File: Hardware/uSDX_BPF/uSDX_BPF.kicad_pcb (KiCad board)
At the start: 2 copper layers, 44.5 x 14 mm, 18 parts

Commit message: updated the 3D models
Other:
- net class Default removed

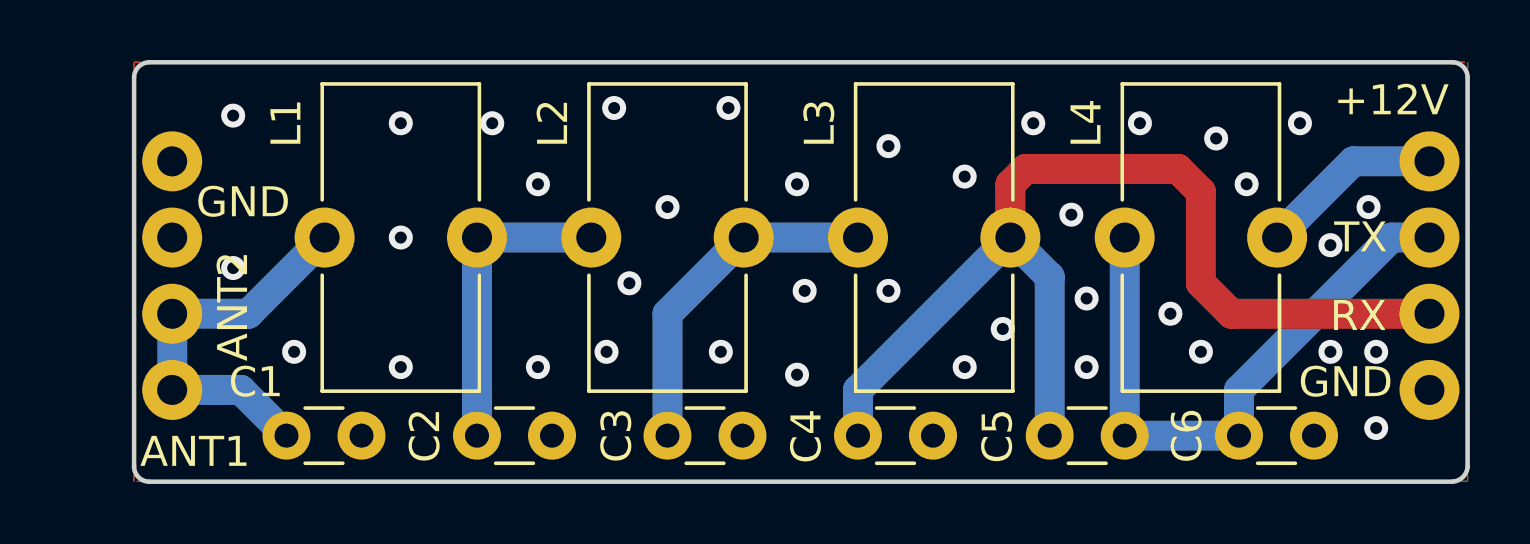
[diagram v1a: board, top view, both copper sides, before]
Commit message: updated the project with transferrable libraries
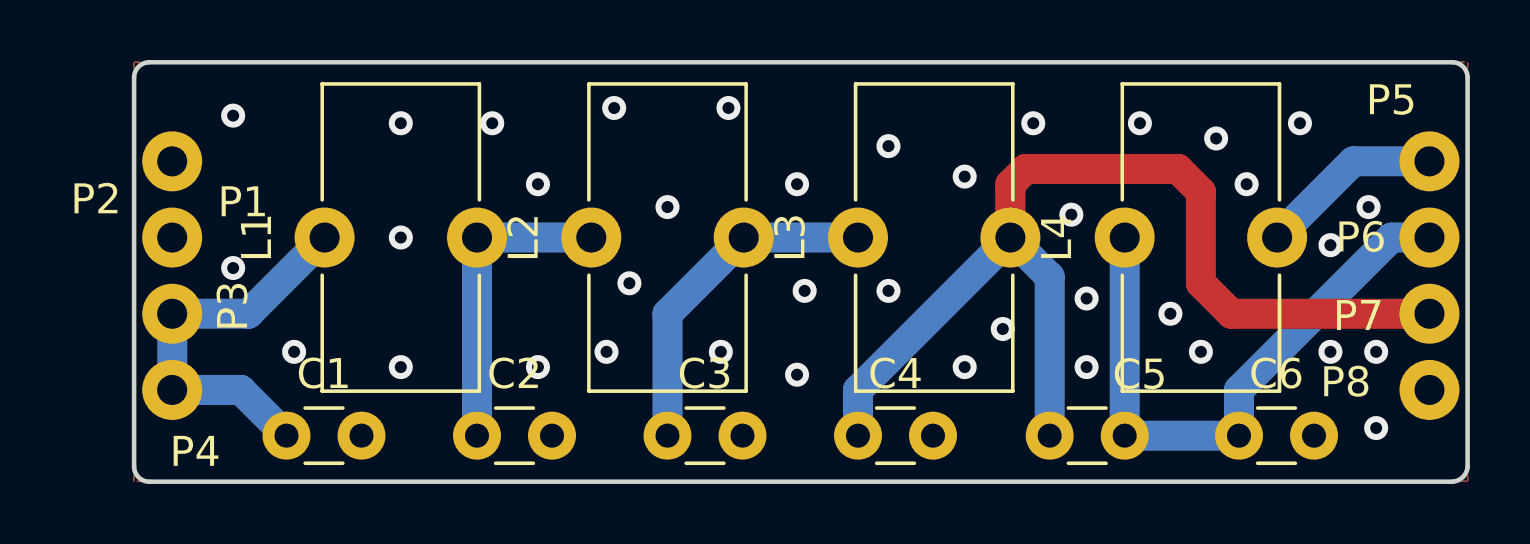
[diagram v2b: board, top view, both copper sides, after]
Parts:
- C1, C2: footprint Capacitor_THT:C_Disc_D3.0mm_W1.6mm_P2.50mm -> user_footprints:C_Disc_D3.0mm_W1.6mm_P2.50mm
- C3: value (none) -> 390pF; footprint Capacitor_THT:C_Disc_D3.0mm_W1.6mm_P2.50mm -> user_footprints:C_Disc_D3.0mm_W1.6mm_P2.50mm
- C4: value (none) -> 180pF; footprint Capacitor_THT:C_Disc_D3.0mm_W1.6mm_P2.50mm -> user_footprints:C_Disc_D3.0mm_W1.6mm_P2.50mm
- C5: value (none) -> 100nF; footprint Capacitor_THT:C_Disc_D3.0mm_W1.6mm_P2.50mm -> user_footprints:C_Disc_D3.0mm_W1.6mm_P2.50mm
- C6: value (none) -> 30pF; footprint Capacitor_THT:C_Disc_D3.0mm_W1.6mm_P2.50mm -> user_footprints:C_Disc_D3.0mm_W1.6mm_P2.50mm
- L1, L2, L3: footprint Inductor_THT:L_Toroid_Vertical_L10.0mm_W5.0mm_P5.08mm -> user_footprints:L_Toroid_Vertical_L10.0mm_W5.0mm_P5.08mm
- L4: value (none) -> T50-2 (9T); footprint Inductor_THT:L_Toroid_Vertical_L10.0mm_W5.0mm_P5.08mm -> user_footprints:L_Toroid_Vertical_L10.0mm_W5.0mm_P5.08mm
- P1, P8: renamed from GND; value (none) -> GND
- P2: renamed from  ; value (none) -> GND
- P3: renamed from ANT2; value (none) -> ANT2
- P4: renamed from ANT1; value (none) -> ANT1
- P5: renamed from +12V; value (none) -> +12V
- P7: renamed from RX; value (none) -> RX
- renumbered TX to P6

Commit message: update library locations
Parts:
- moved P5 2.70 mm to (97.8, 36.5)
- moved P6 1.10 mm to (97.8, 39.1)
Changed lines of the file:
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@@
   )
   (footprint "user_footprints:pin" (layer "F.Cu")
-    (at 95.09 36.5252)
-    (property "Sheetfile" "uSDX_BPF.kicad_sch")
-    (property "Sheetname" "")
-    (attr through_hole)
-    (fp_text reference "P5" (at 1.43 -2.2352) (layer "F.SilkS")
-      (effects (font (size 1 1) (thickness 0.15)))
-    )
-    (fp_text value "+12V" (at -4.91 -1.3932) (layer "F.Fab")
-      (effects (font (size 1 1) (thickness 0.15)))
-    )
-    (pad "1" thru_hole circle locked (at 2.7 -0.2032) (size 2 2) (drill 1) (layers *.Cu *.Mask)
+    (at 97.79 36.5252)
+    (property "Sheetfile" "uSDX_BPF.kicad_sch")
+    (property "Sheetname" "")
+    (attr through_hole)
+    (fp_text reference "P5" (at 0 -2.54) (layer "F.SilkS")
+      (effects (font (size 0.8 0.8) (thickness 0.1)))
+    )
+    (fp_text value "+12V" (at 0 -5.08) (layer "F.Fab")
+      (effects (font (size 0.8 0.8) (thickness 0.1)))
+    )
+    (pad "1" thru_hole circle (at 0 -0.2032) (size 2 2) (drill 1) (layers *.Cu *.Mask)
       (net 7 "Net-(L4-Pad2)") (pintype "unspecified"))
-    (model "C:/Users/Liviu/Documents/Projects/uSDX_variant/Hardware/3D_models/filterStandoff.step"
-      (offset (xyz 2.7 0 0))
+    (model "${KICAD6_3DMODEL_DIR}/filterStandoff.step"
+      (offset (xyz 0 0 0))
       (scale (xyz 1 1 1))
       (rotate (xyz 0 0 0))
@@
     (property "Sheetname" "")
     (attr through_hole)
-    (fp_text reference "P7" (at -2.37 -0.1232) (layer "F.SilkS")
-      (effects (font (size 1 1) (thickness 0.15)))
-    )
-    (fp_text value "RX" (at -3.64 -0.1232) (layer "F.Fab")
-      (effects (font (size 1 1) (thickness 0.15)))
-    )
-    (pad "1" thru_hole circle locked (at 0 -0.2032) (size 2 2) (drill 1) (layers *.Cu *.Mask)
+    (fp_text reference "P7" (at 0 -2.54) (layer "F.SilkS")
+      (effects (font (size 0.8 0.8) (thickness 0.1)))
+    )
+    (fp_text value "RX" (at 0 -5.08) (layer "F.Fab")
+      (effects (font (size 0.8 0.8) (thickness 0.1)))
+    )
+    (pad "1" thru_hole circle (at 0 -0.2032) (size 2 2) (drill 1) (layers *.Cu *.Mask)
       (net 5 "Net-(C4-Pad1)") (pintype "unspecified"))
-    (model "C:/Users/Liviu/Documents/Projects/uSDX_variant/Hardware/3D_models/filterStandoff.step"
+    (model "${KICAD6_3DMODEL_DIR}/filterStandoff.step"
       (offset (xyz 0 0 0))
       (scale (xyz 1 1 1))
@@
     (property "Sheetname" "")
     (attr through_hole)
-    (fp_text reference "P8" (at -2.794 -0.4572) (layer "F.SilkS")
-      (effects (font (size 1 1) (thickness 0.15)))
-    )
-    (fp_text value "GND" (at -2.37 -0.1232) (layer "F.Fab")
-      (effects (font (size 1 1) (thickness 0.15)))
-    )
-    (pad "1" thru_hole circle locked (at 0 -0.2032) (size 2 2) (drill 1) (layers *.Cu *.Mask)
+    (fp_text reference "P8" (at 0 -2.54) (layer "F.SilkS")
+      (effects (font (size 0.8 0.8) (thickness 0.1)))
+    )
+    (fp_text value "GND" (at 0 -5.08) (layer "F.Fab")
+      (effects (font (size 0.8 0.8) (thickness 0.1)))
+    )
+    (pad "1" thru_hole circle (at 0 -0.2032) (size 2 2) (drill 1) (layers *.Cu *.Mask)
       (net 1 "GND") (pintype "unspecified"))
     (model "${KICAD6_3DMODEL_DIR}/filterStandoff.step"
@@
     (property "Sheetname" "")
     (attr through_hole)
-    (fp_text reference "P4" (at 0.765353 1.864672) (layer "F.SilkS")
-      (effects (font (size 1 1) (thickness 0.15)))
-    )
-    (fp_text value "ANT1" (at -3.81 -0.2032) (layer "F.Fab")
-      (effects (font (size 1 1) (thickness 0.15)))
-    )
-    (pad "1" thru_hole circle locked (at 0 -0.2032) (size 2 2) (drill 1) (layers *.Cu *.Mask)
+    (fp_text reference "P4" (at 0 -2.54) (layer "F.SilkS")
+      (effects (font (size 0.8 0.8) (thickness 0.1)))
+    )
+    (fp_text value "ANT1" (at 0 -5.08) (layer "F.Fab")
+      (effects (font (size 0.8 0.8) (thickness 0.1)))
+    )
+    (pad "1" thru_hole circle (at 0 -0.2032) (size 2 2) (drill 1) (layers *.Cu *.Mask)
       (net 2 "Net-(C1-Pad1)") (pintype "unspecified"))
-    (model "C:/Users/Liviu/Documents/Projects/uSDX_variant/Hardware/3D_models/filterStandoff.step"
+    (model "${KICAD6_3DMODEL_DIR}/filterStandoff.step"
       (offset (xyz 0 0 0))
       (scale (xyz 1 1 1))
@@
     (property "Sheetname" "")
     (attr through_hole)
-    (fp_text reference "P2" (at -2.54 -1.4732) (layer "F.SilkS")
-      (effects (font (size 1 1) (thickness 0.15)))
-    )
-    (fp_text value "GND" (at -2.54 -0.2032) (layer "F.Fab")
-      (effects (font (size 1 1) (thickness 0.15)))
-    )
-    (pad "1" thru_hole circle locked (at 0 -0.2032) (size 2 2) (drill 1) (layers *.Cu *.Mask)
+    (fp_text reference "P2" (at 0 -2.54) (layer "F.SilkS")
+      (effects (font (size 0.8 0.8) (thickness 0.1)))
+    )
+    (fp_text value "GND" (at 0 -5.08) (layer "F.Fab")
+      (effects (font (size 0.8 0.8) (thickness 0.1)))
+    )
+    (pad "1" thru_hole circle (at 0 -0.2032) (size 2 2) (drill 1) (layers *.Cu *.Mask)
       (net 1 "GND") (pintype "unspecified"))
-    (model "C:/Users/Liviu/Documents/Projects/uSDX_variant/Hardware/3D_models/filterStandoff.step"
-      (offset (xyz 0 0 0))
-      (scale (xyz 1 1 1))
-      (rotate (xyz 0 0 0))
-    )
-  )
-  (footprint "user_footprints:pin" (layer "F.Cu")
-    (at 96.69 39.0652)
-    (property "Sheetfile" "uSDX_BPF.kicad_sch")
-    (property "Sheetname" "")
-    (attr through_hole)
-    (fp_text reference "P6" (at -1.186 -0.2032) (layer "F.SilkS")
-      (effects (font (size 1 1) (thickness 0.15)))
-    )
-    (fp_text value "TX" (at -3.64 -0.1232) (layer "F.Fab")
-      (effects (font (size 1 1) (thickness 0.15)))
-    )
-    (pad "1" thru_hole circle locked (at 1.1 -0.2032) (size 2 2) (drill 1) (layers *.Cu *.Mask)
+    (model "${KICAD6_3DMODEL_DIR}/filterStandoff.step"
+      (offset (xyz 0 0 0))
+      (scale (xyz 1 1 1))
+      (rotate (xyz 0 0 0))
+    )
+  )
+  (footprint "user_footprints:pin" (layer "F.Cu")
+    (at 97.79 39.0652)
+    (property "Sheetfile" "uSDX_BPF.kicad_sch")
+    (property "Sheetname" "")
+    (attr through_hole)
+    (fp_text reference "P6" (at 0 -2.54) (layer "F.SilkS")
+      (effects (font (size 0.8 0.8) (thickness 0.1)))
+    )
+    (fp_text value "TX" (at 0 -5.08) (layer "F.Fab")
+      (effects (font (size 0.8 0.8) (thickness 0.1)))
+    )
+    (pad "1" thru_hole circle (at 0 -0.2032) (size 2 2) (drill 1) (layers *.Cu *.Mask)
       (net 6 "Net-(C5-Pad1)") (pintype "unspecified"))
-    (model "C:/Users/Liviu/Documents/Projects/uSDX_variant/Hardware/3D_models/filterStandoff.step"
-      (offset (xyz 1.1 0 0))
+    (model "${KICAD6_3DMODEL_DIR}/filterStandoff.step"
+      (offset (xyz 0 0 0))
       (scale (xyz 1 1 1))
       (rotate (xyz 0 0 0))
@@
     (property "Sheetname" "")
     (attr through_hole)
-    (fp_text reference "P1" (at 2.365346 1.164703 180) (layer "F.SilkS")
-      (effects (font (size 1 1) (thickness 0.15)))
-    )
-    (fp_text value "GND" (at -2.54 -1.4732) (layer "F.Fab")
-      (effects (font (size 1 1) (thickness 0.15)))
-    )
-    (pad "1" thru_hole circle locked (at 0 -0.2032) (size 2 2) (drill 1) (layers *.Cu *.Mask)
+    (fp_text reference "P1" (at 0 -2.54) (layer "F.SilkS")
+      (effects (font (size 0.8 0.8) (thickness 0.1)))
+    )
+    (fp_text value "GND" (at 0 -5.08) (layer "F.Fab")
+      (effects (font (size 0.8 0.8) (thickness 0.1)))
+    )
+    (pad "1" thru_hole circle (at 0 -0.2032) (size 2 2) (drill 1) (layers *.Cu *.Mask)
       (net 1 "GND") (pintype "unspecified"))
-    (model "C:/Users/Liviu/Documents/Projects/uSDX_variant/Hardware/3D_models/filterStandoff.step"
+    (model "${KICAD6_3DMODEL_DIR}/filterStandoff.step"
       (offset (xyz 0 0 0))
       (scale (xyz 1 1 1))
@@
     (property "Sheetname" "")
     (attr through_hole)
-    (fp_text reference "P3" (at 2.032 -0.4572 90) (layer "F.SilkS")
-      (effects (font (size 1 1) (thickness 0.15)))
-    )
-    (fp_text value "ANT2" (at -5.08 -0.2032) (layer "F.Fab")
-      (effects (font (size 1 1) (thickness 0.15)))
-    )
-    (pad "1" thru_hole circle locked (at 0 -0.2032) (size 2 2) (drill 1) (layers *.Cu *.Mask)
+    (fp_text reference "P3" (at 0 -2.54) (layer "F.SilkS")
+      (effects (font (size 0.8 0.8) (thickness 0.1)))
+    )
+    (fp_text value "ANT2" (at 0 -5.08) (layer "F.Fab")
+      (effects (font (size 0.8 0.8) (thickness 0.1)))
+    )
+    (pad "1" thru_hole circle (at 0 -0.2032) (size 2 2) (drill 1) (layers *.Cu *.Mask)
       (net 2 "Net-(C1-Pad1)") (pintype "unspecified"))
-    (model "C:/Users/Liviu/Documents/Projects/uSDX_variant/Hardware/3D_models/filterStandoff.step"
-      (offset (xyz 0 0 0))
-      (scale (xyz 1 1 1))
+    (model "${KICAD6_3DMODEL_DIR}/filterStandoff.step"
+      (offset (xyz 0 0 0))
+      (scale (xyz 1 1 1))
